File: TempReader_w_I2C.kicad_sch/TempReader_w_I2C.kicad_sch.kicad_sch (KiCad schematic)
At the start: 42 parts, among them J1 NRF Pin Header, J2 BME Pin Header, U5 MIC5205-3.3YM5, Y1 16MH

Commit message: Added debug prints for UART
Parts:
- removed Y1: 16MH, ECS-160-20-46X:XTAL_ECS-160-20-46X, symbol Device:Crystal
- added B1: BS-3, BS-3_MPD, symbol BS-3:BS-3
- added C16: 10uF, Capacitor_SMD:C_0603_1608Metric_Pad1.08x0.95mm_HandSolder, symbol Device:C
- added J3: PowerHeader, Connector_PinHeader_1.27mm:PinHeader_1x02_P1.27mm_Vertical, symbol Connector_Generic:Conn_01x02
- added Y2: 16Mhz, ECS-160-12-4X-GM:XTAL_ECS-160-12-4X-GM, symbol ECS-160-12-4X-GM:ECS-160-12-4X-GM
- renumbered NotSure1 to STLinkHeader1
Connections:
- net +3V3: now also C16.2
- net GND1: now also B1.1, C16.1, J3.1 (Pin_1)
- net PowerIn: now also B1.2, J3.2 (Pin_2)
- net at C14.1, NRF24L01+1.9 (XC2), R2.1: now also Y2.1
- net at C15.1, NRF24L01+1.10 (XC1), R2.2: now also Y2.2
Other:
- moved on the sheet: C15, R2

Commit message: Slightly change comments
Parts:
- added C17: 100 nF, Capacitor_SMD:C_0603_1608Metric_Pad1.08x0.95mm_HandSolder, symbol Device:C
- added D1: WL-SMCW_0603, footprints:WL-SMCW_0603, symbol 150060GS75000:WL-SMCW_0603
- added R12: 165, Resistor_SMD:R_0603_1608Metric, symbol Device:R
- added SW1: D6R90F2LFS, D6R90_CNK, symbol D6R90:D6R90F2LFS
- B1: footprint BS-3_MPD -> footprints:BS-3_MPD
- C7: value 1u -> 1uF
- J1: footprint Connector_PinHeader_2.54mm:PinHeader_2x04_P2.54mm_Vertical -> footprints:CON8_2X4_TU_SSQ
- J3: footprint Connector_PinHeader_1.27mm:PinHeader_1x02_P1.27mm_Vertical -> Connector_PinHeader_2.54mm:PinHeader_1x02_P2.54mm_Vertical
- R5: value 0 -> 10k
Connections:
- net +3V3: now also J1.1 (Pin_1); no longer J1.4 (Pin_4)
- net GND1: now also J1.2 (Pin_2), C17.2, D1.1, SW1.3; no longer J1.5 (Pin_5)
- net I2C_SDA: now also J2.2 (Pin_2); no longer J2.3 (Pin_3)
- net NRF_CE: now also J1.4 (Pin_4); no longer J1.6 (Pin_6)
- net NRF_IRQ: now also J1.7 (Pin_7); no longer J1.1 (Pin_1)
- net NRST: now also C17.1, SW1.4
- net SPI_MOSI: now also J1.5 (Pin_5); no longer J1.2 (Pin_2)
- net SPI_SCK: now also J1.6 (Pin_6); no longer J1.7 (Pin_7)
- net BME_CSB: now reaches BME280.2 (CSB)
- net BME_CSB: now also J2.1 (Pin_1)
- net BME_SDO: now reaches BME280.5 (SDO)
- net BME_SDO: now also J2.3 (Pin_3)
- new net: D1.2, R12.2
- no-connect marks 19 -> 17
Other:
- moved on the sheet: BME280, C4, C8, J2, R10, R11, R3, R4, R5, R6, R7, R9

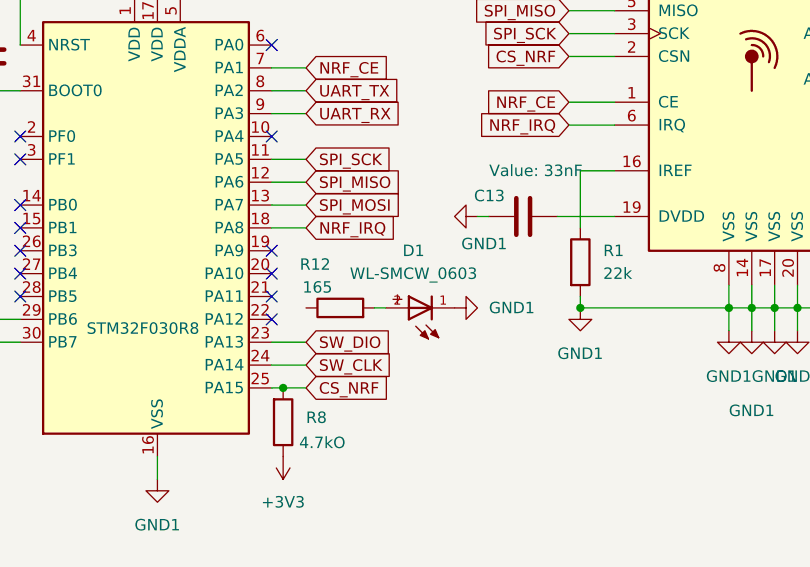
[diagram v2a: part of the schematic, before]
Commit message: Remove functionality to test UART
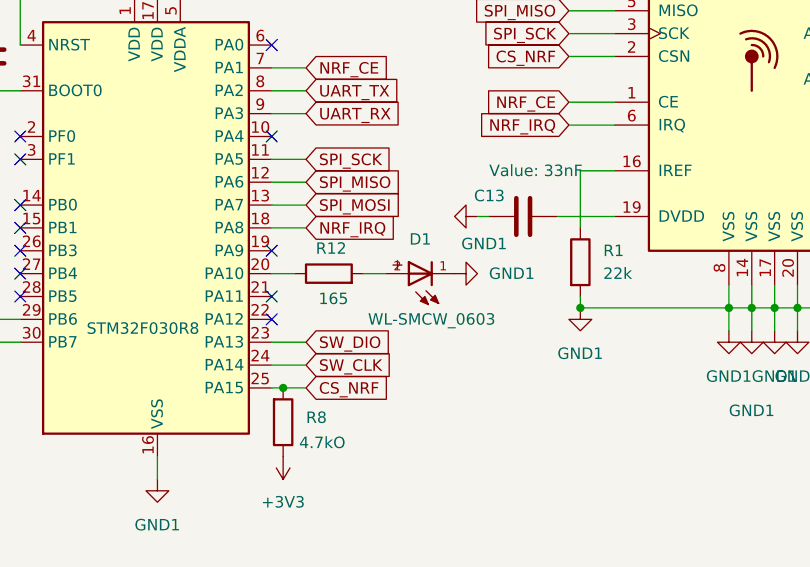
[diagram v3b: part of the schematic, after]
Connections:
- net at R12.1: now also STM32F030R8.20 (PA10)
- no-connect marks 17 -> 16
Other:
- moved on the sheet: D1, R12
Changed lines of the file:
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@@
 	)
 	(no_connect
-		(at 151.13 109.22)
-	)
-	(no_connect
 		(at 43.18 38.1)
 	)
@@
 	(wire
 		(pts
+			(xy 153.67 109.22) (xy 151.13 109.22)
+		)
+		(stroke
+			(width 0)
+			(type default)
+		)
+	)
+	(wire
+		(pts
 			(xy 200.66 50.8) (xy 204.47 50.8)
 		)
@@
 	(wire
 		(pts
-			(xy 162.56 113.03) (xy 163.83 113.03)
+			(xy 161.29 109.22) (xy 163.83 109.22)
 		)
 		(stroke
@@
 	(symbol
 		(lib_id "Device:R")
-		(at 158.75 113.03 90)
+		(at 157.48 109.22 90)
 		(unit 1)
 		(exclude_from_sim no)
@@
 		(dnp no)
 		(property "Reference" "R12"
-			(at 155.956 108.204 90)
+			(at 157.734 106.426 90)
 			(effects
 				(font
@@
 		)
 		(property "Value" "165"
-			(at 156.21 110.744 90)
+			(at 157.988 112.014 90)
 			(effects
 				(font
@@
 		)
 		(property "Footprint" "Resistor_SMD:R_0603_1608Metric"
-			(at 158.75 114.808 90)
+			(at 157.48 110.998 90)
 			(effects
 				(font
@@
 		)
 		(property "Datasheet" "~"
-			(at 158.75 113.03 0)
+			(at 157.48 109.22 0)
 			(effects
 				(font
@@
 		)
 		(property "Description" "Resistor"
-			(at 158.75 113.03 0)
+			(at 157.48 109.22 0)
 			(effects
 				(font
@@
 	(symbol
 		(lib_id "power:GND1")
-		(at 171.45 113.03 90)
+		(at 171.45 109.22 90)
 		(unit 1)
 		(exclude_from_sim no)
@@
 		(fields_autoplaced yes)
 		(property "Reference" "#PWR046"
-			(at 177.8 113.03 0)
+			(at 177.8 109.22 0)
 			(effects
 				(font
@@
 		)
 		(property "Value" "GND1"
-			(at 175.26 113.0299 90)
+			(at 175.26 109.2199 90)
 			(effects
 				(font
@@
 		)
 		(property "Footprint" ""
-			(at 171.45 113.03 0)
+			(at 171.45 109.22 0)
 			(effects
 				(font
@@
 		)
 		(property "Datasheet" ""
-			(at 171.45 113.03 0)
+			(at 171.45 109.22 0)
 			(effects
 				(font
@@
 		)
 		(property "Description" "Power symbol creates a global label with name \"GND1\" , ground"
-			(at 171.45 113.03 0)
+			(at 171.45 109.22 0)
 			(effects
 				(font
@@
 	(symbol
 		(lib_id "150060GS75000:WL-SMCW_0603")
-		(at 168.91 113.03 180)
+		(at 168.91 109.22 180)
 		(unit 1)
 		(exclude_from_sim no)
@@
 		(on_board yes)
 		(dnp no)
-		(fields_autoplaced yes)
 		(property "Reference" "D1"
-			(at 166.8917 106.68 0)
+			(at 167.64 105.41 0)
 			(effects
 				(font
@@
 		)
 		(property "Value" "WL-SMCW_0603"
-			(at 166.8917 109.22 0)
+			(at 168.91 114.3 0)
 			(effects
 				(font
@@
 		)
 		(property "Footprint" "footprints:WL-SMCW_0603"
-			(at 168.91 113.03 0)
+			(at 168.91 109.22 0)
 			(effects
 				(font
@@
 		)
 		(property "Datasheet" ""
-			(at 168.91 113.03 0)
+			(at 168.91 109.22 0)
 			(effects
 				(font
@@
 		)
 		(property "Description" ""
-			(at 168.91 113.03 0)
+			(at 168.91 109.22 0)
 			(effects
 				(font

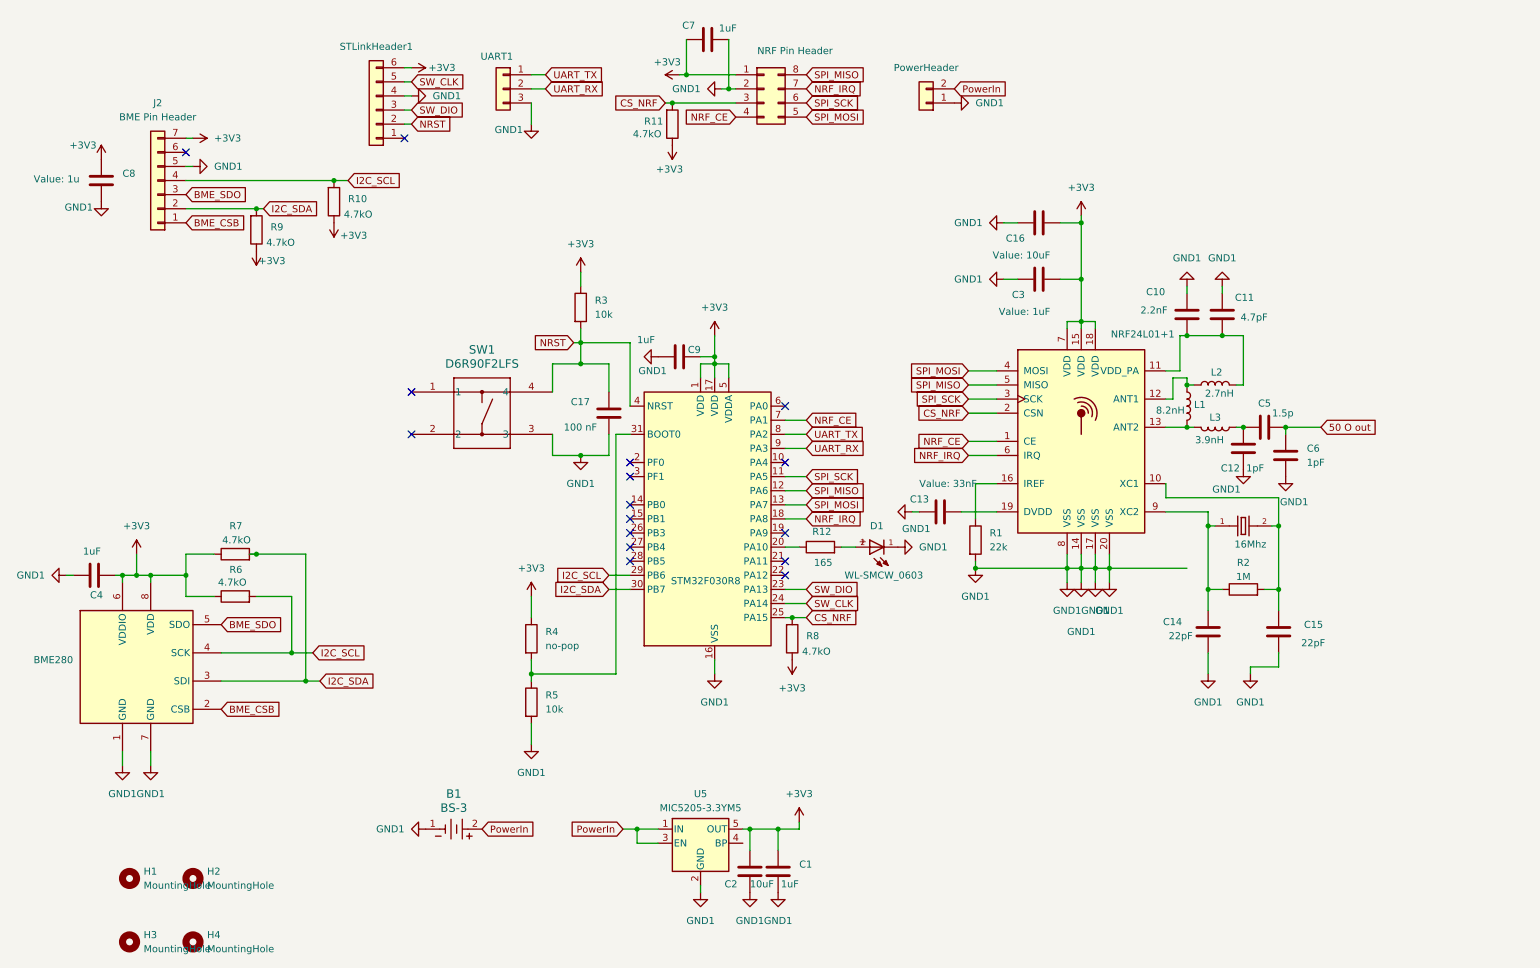
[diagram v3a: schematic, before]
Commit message: Change UART pins again
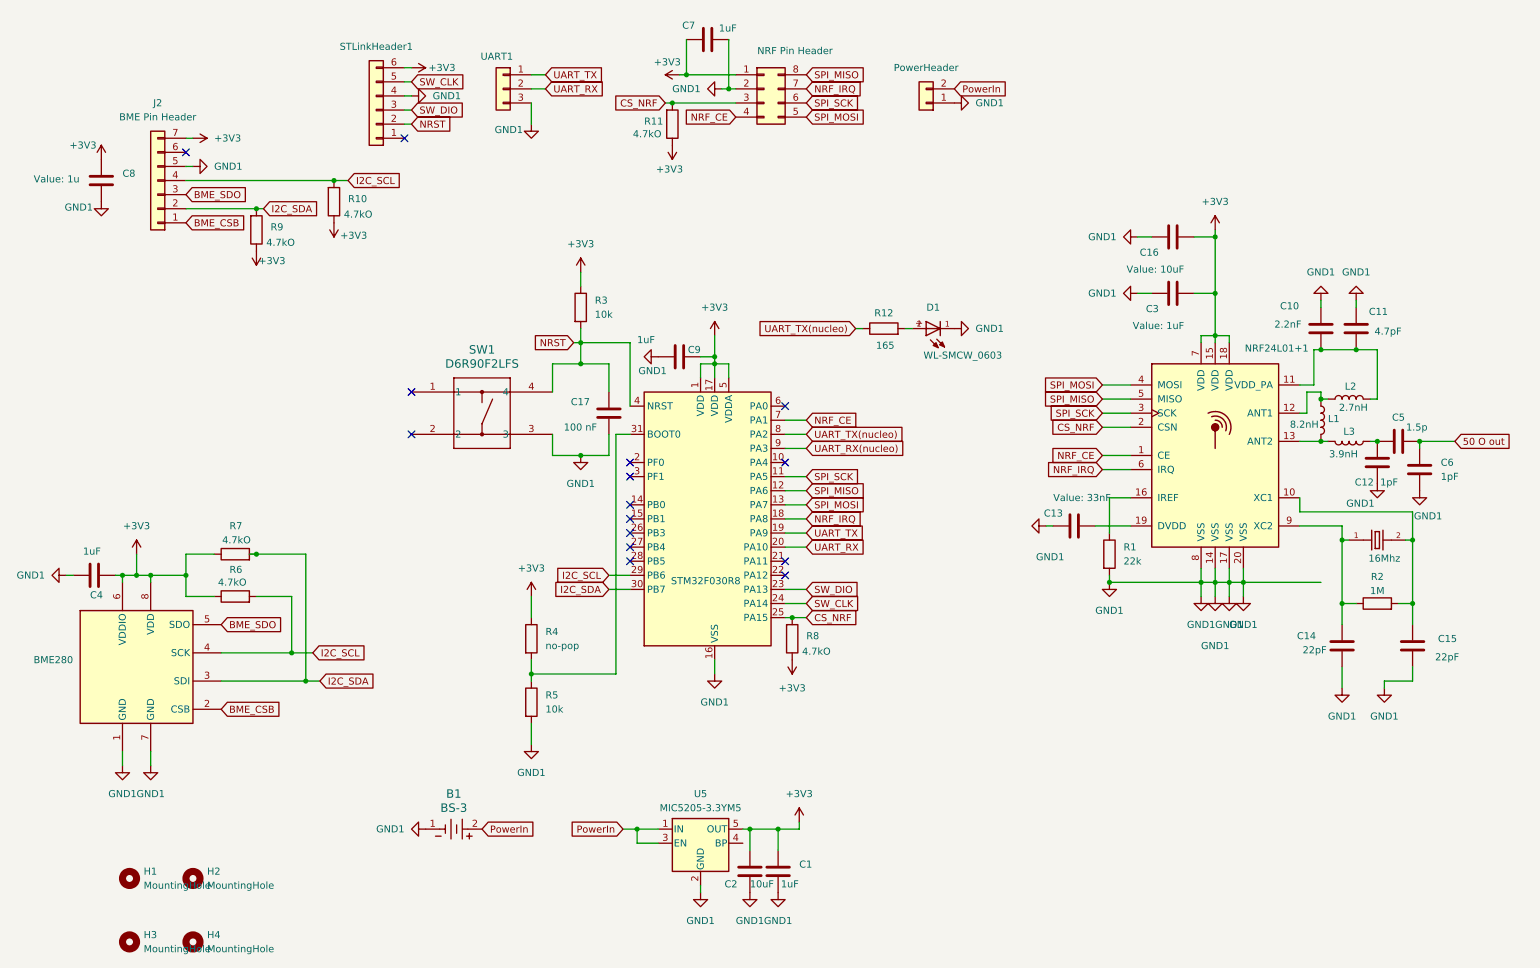
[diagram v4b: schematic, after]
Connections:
- net UART_RX: now also STM32F030R8.20 (PA10); no longer STM32F030R8.9 (PA3)
- net UART_TX: now also STM32F030R8.19 (PA9); no longer STM32F030R8.8 (PA2)
- net UART_TX(nucleo): now reaches R12.1
- net UART_TX(nucleo): now also STM32F030R8.8 (PA2); no longer STM32F030R8.20 (PA10)
- new net UART_RX(nucleo): STM32F030R8.9 (PA3)
- no-connect marks 16 -> 15
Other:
- moved on the sheet: C10, C11, C12, C13, C14, C15, C16, C3, C5, C6, L1, L2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

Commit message: Changed RAM settings in config
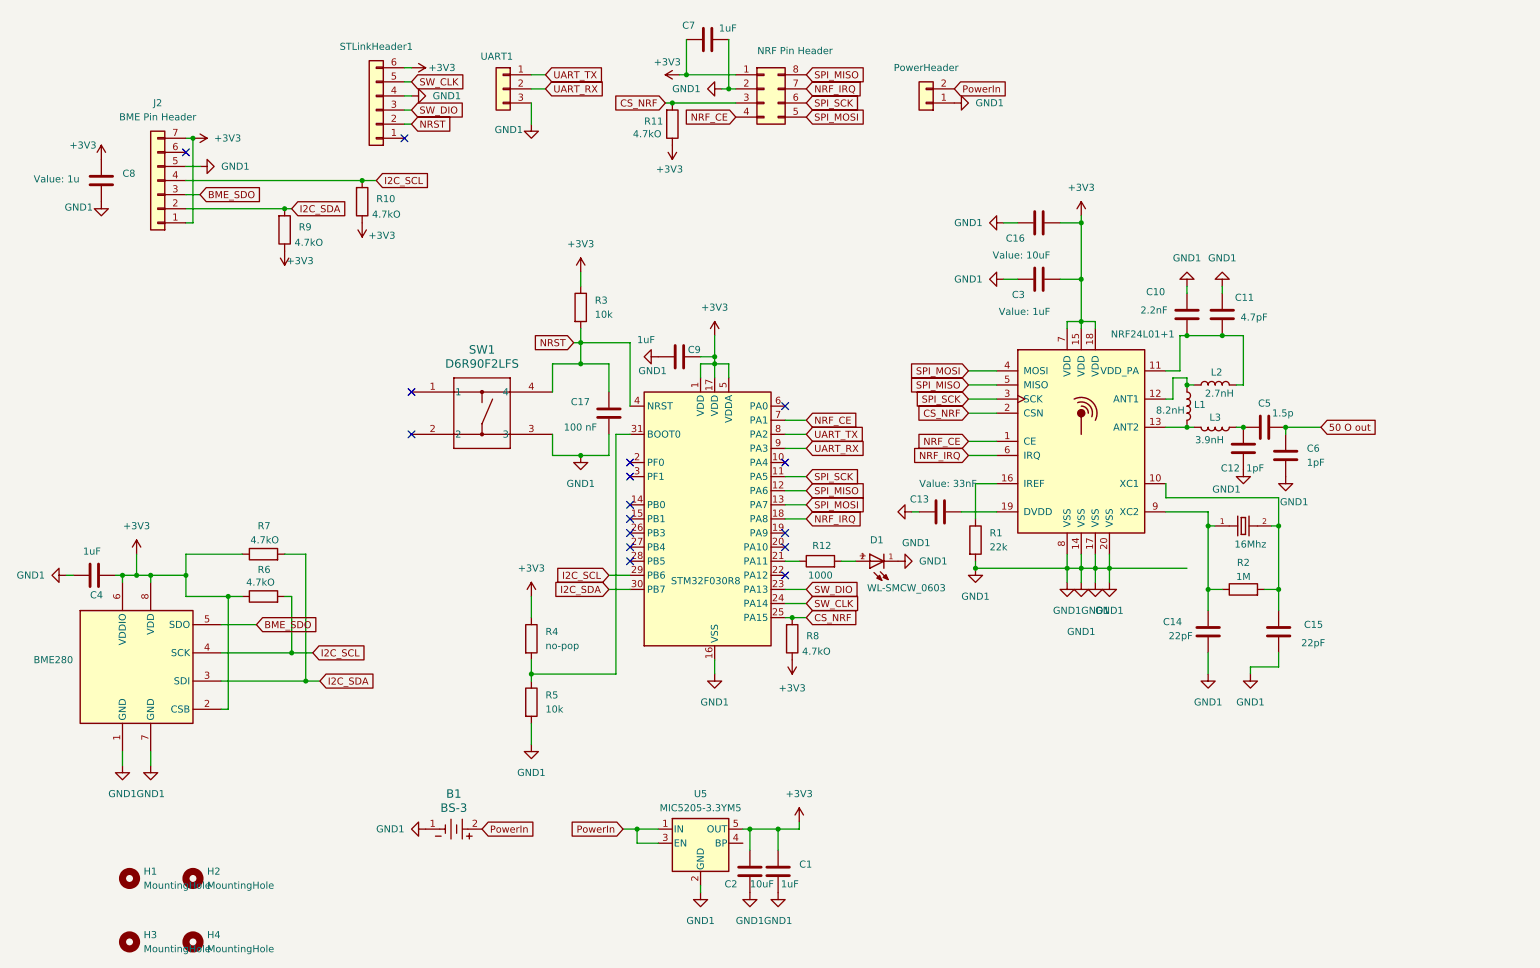
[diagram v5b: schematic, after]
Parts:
- R12: value 165 -> 1000
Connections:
- net BME_CSB is gone; now on net +3V3: BME280.2 (CSB), J2.1 (Pin_1)
- net UART_RX(nucleo) is gone; now on net UART_RX: STM32F030R8.9 (PA3)
- net UART_RX: no longer STM32F030R8.20 (PA10)
- net UART_TX: now also STM32F030R8.8 (PA2); no longer STM32F030R8.19 (PA9)
- net at STM32F030R8.21 (PA11): now also R12.1
- removed net UART_TX(nucleo): R12.1, STM32F030R8.8 (PA2)
- no-connect marks 15 -> 16
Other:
- moved on the sheet: C10, C11, C12, C13, C14, C15, C16, C3, C5, C6, L1, L2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

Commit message: Nucleo branch created
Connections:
- net BME_SDO is gone; now on net GND1: BME280.5 (SDO), J2.3 (Pin_3)
